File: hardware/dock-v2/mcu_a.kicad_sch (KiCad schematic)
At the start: 29 parts, among them SW301 SW_Push, SW302 SW_Push, U301 RP2354A, Y301 12MHz

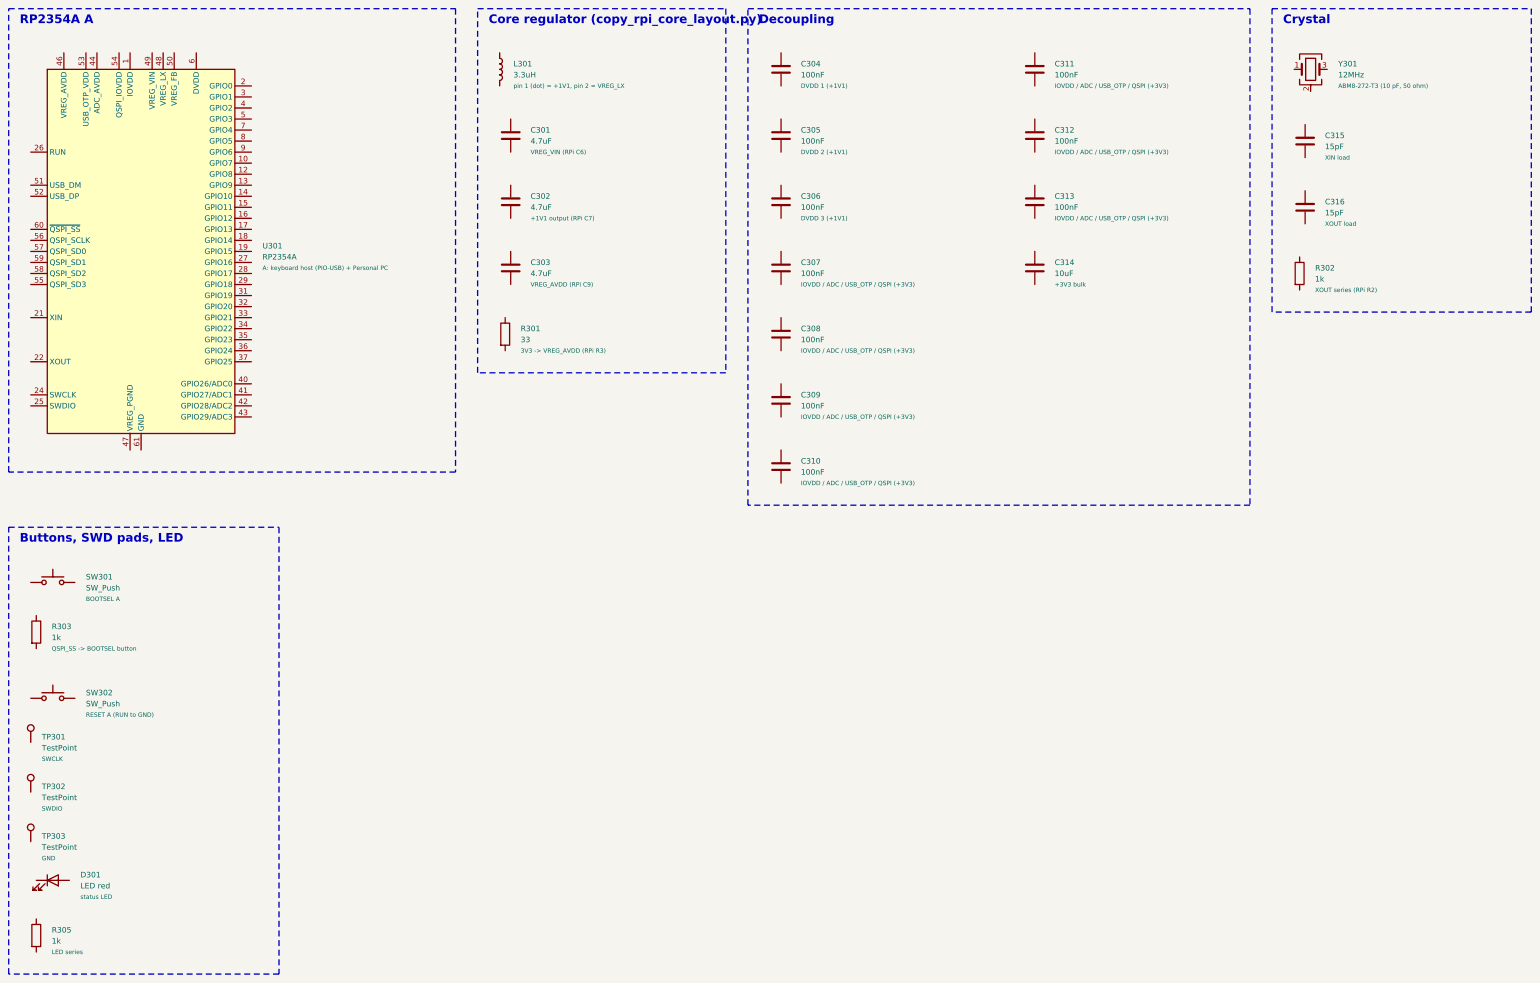
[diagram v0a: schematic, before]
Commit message: Dock v2 schematic: wiring in progress (user's work, snapshot before fixes)
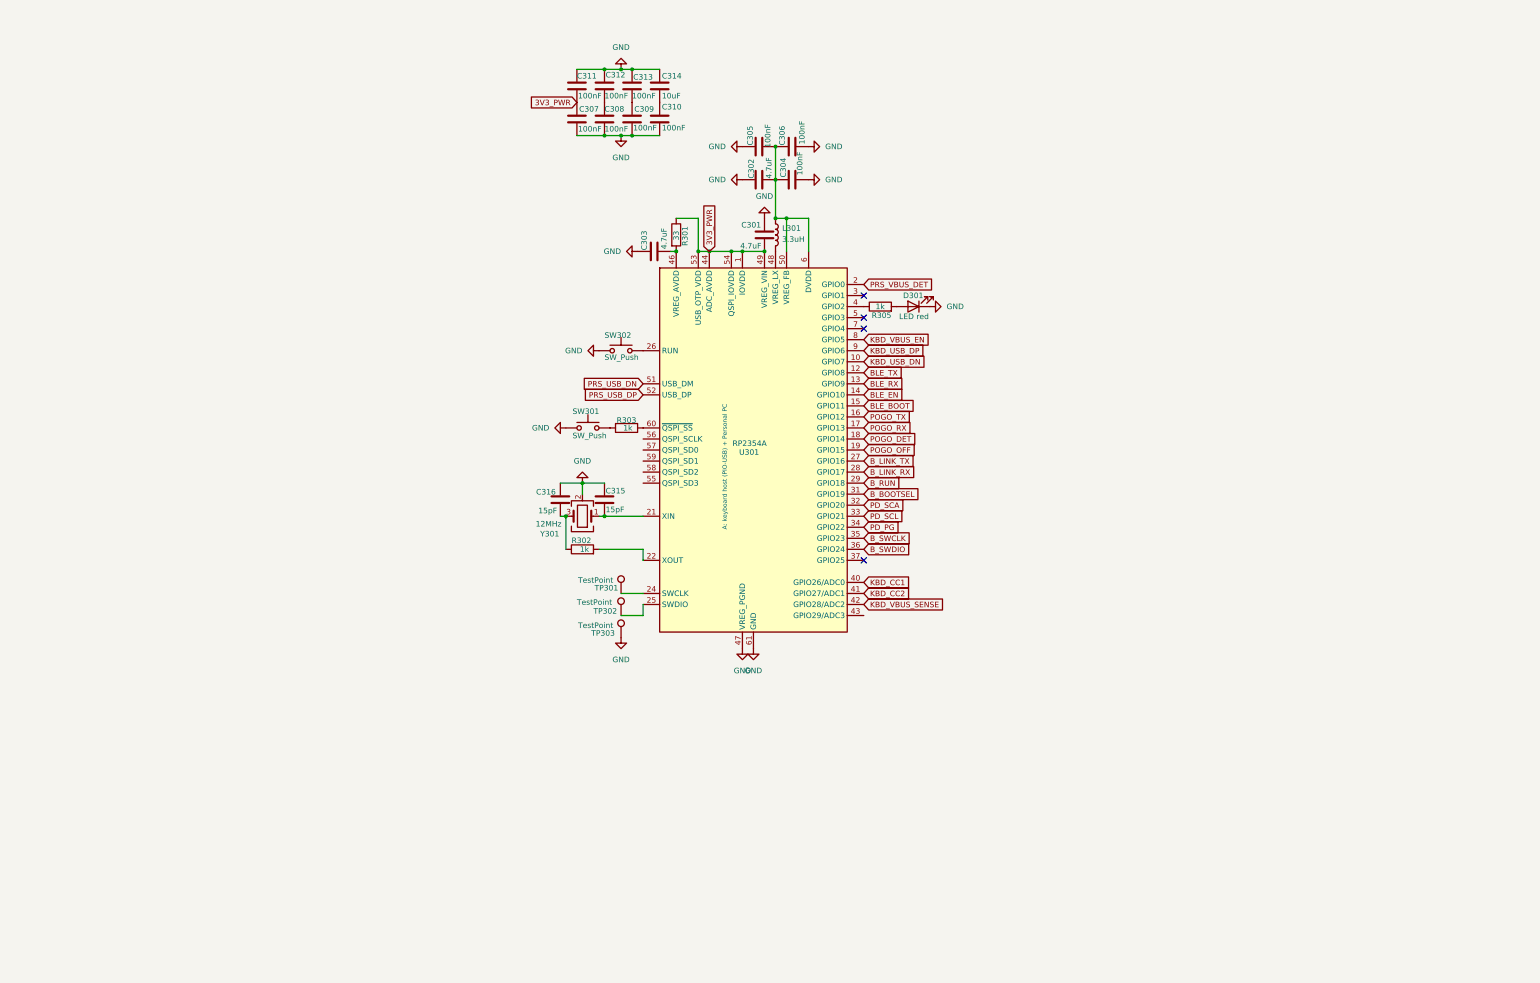
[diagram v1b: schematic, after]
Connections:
- net 3V3_PWR: now reaches R301.1
- net 3V3_PWR: now also C301.2, C307.1, C311.2, U301.1 (IOVDD), U301.11 (IOVDD), U301.20 (IOVDD), U301.30 (IOVDD), U301.38 (IOVDD), U301.44 (ADC_AVDD), U301.45 (IOVDD), U301.49 (VREG_VIN), U301.53 (USB_OTP_VDD), U301.54 (QSPI_IOVDD)
- net at R301.2: now also C303.2, U301.46 (VREG_AVDD)
- net at C309.1: now also C313.2
- net GND: now reaches C309.2
- net GND: now also C301.1, C302.1, C303.1, C304.2, C305.1, C306.2, C307.2, C308.2, C310.2, C311.1, C312.1, C313.1, C314.1, C315.1, C316.1, D301.1 (K), SW301.1, SW302.1, TP303.1, U301.47 (VREG_PGND), U301.61 (GND), Y301.2 (G), Y301.4 (G)
- net at D301.2 (A): now also R305.2
- net KBD_USB_DN: now reaches U301.10 (GPIO7)
- net BLE_TX: now reaches U301.12 (GPIO8)
- net BLE_RX: now reaches U301.13 (GPIO9)
- net BLE_EN: now reaches U301.14 (GPIO10)
- net BLE_BOOT: now reaches U301.15 (GPIO11)
- net POGO_TX: now reaches U301.16 (GPIO12)
- net POGO_RX: now reaches U301.17 (GPIO13)
- net POGO_DET: now reaches U301.18 (GPIO14)
- net POGO_OFF: now reaches U301.19 (GPIO15)
- net PRS_VBUS_DET: now reaches U301.2 (GPIO0)
- net at U301.21 (XIN): now also C315.2, Y301.1
- net at U301.22 (XOUT): now also R302.2
- net at U301.23 (DVDD), U301.39 (DVDD), U301.6 (DVDD): now also C302.2, C304.1, C305.2, C306.1, L301.1, U301.50 (VREG_FB)
- net at U301.24 (SWCLK): now also TP301.1
- net at U301.25 (SWDIO): now also TP302.1
- net at U301.26 (RUN): now also SW302.2
- net B_LINK_TX: now reaches U301.27 (GPIO16)
- net B_LINK_RX: now reaches U301.28 (GPIO17)
- net B_RUN: now reaches U301.29 (GPIO18)
- net B_BOOTSEL: now reaches U301.31 (GPIO19)
- net PD_SCA: now reaches U301.32 (GPIO20)
- net PD_SCL: now reaches U301.33 (GPIO21)
- net PD_PG: now reaches U301.34 (GPIO22)
- net B_SWCLK: now reaches U301.35 (GPIO23)
- net B_SWDIO: now reaches U301.36 (GPIO24)
- net at U301.4 (GPIO2): now also R305.1
- net KBD_CC1: now reaches U301.40 (GPIO26/ADC0)
- net KBD_CC2: now reaches U301.41 (GPIO27/ADC1)
- net KBD_VBUS_SENSE: now reaches U301.42 (GPIO28/ADC2)
- net at U301.48 (VREG_LX): now also L301.2
- net PRS_USB_DN: now reaches U301.51 (USB_DM)
- net PRS_USB_DP: now reaches U301.52 (USB_DP)
- net at U301.60 (~{QSPI_SS}): now also R303.1
- net KBD_VBUS_EN: now reaches U301.8 (GPIO5)
- net KBD_USB_DP: now reaches U301.9 (GPIO6)
- net at C308.1: now also C312.2
- net at SW301.2: now also R303.2
- net at Y301.3: now also C316.2, R302.1
- net at C310.1: now also C314.2
- no-connect marks 0 -> 4
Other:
- note removed: "Buttons, SWD pads, LED"
- note removed: "Core regulator (copy_rpi_core_layout.py)"
- note removed: "Crystal"
- note removed: "Decoupling"
- note removed: "RP2354A A"
